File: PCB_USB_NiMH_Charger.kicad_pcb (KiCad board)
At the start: 2 copper layers, 94.9 x 72 mm, 45 parts, among them J1 USB_C_Receptacle_Simple, J2 Conn_02x01, J3 Conn_02x01, J4 Conn_02x01, Q1 2SA1015, Q2 2SC1815, Q3 2SB834, Q4 2SC1815, Q5 2SB834, U1 LM393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

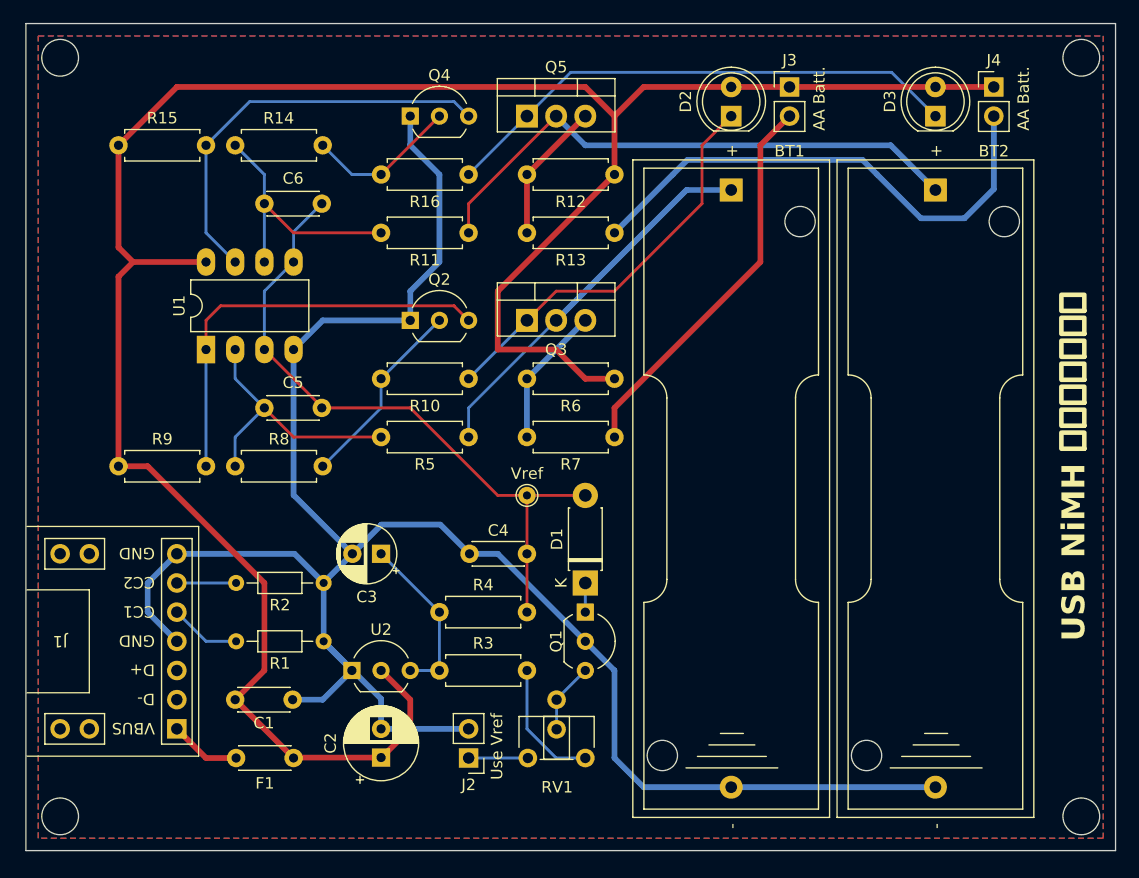
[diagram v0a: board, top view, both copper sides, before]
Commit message: WIP: Change 2-battery circuit to 4-battery circuit
Change LM393 to LM339.
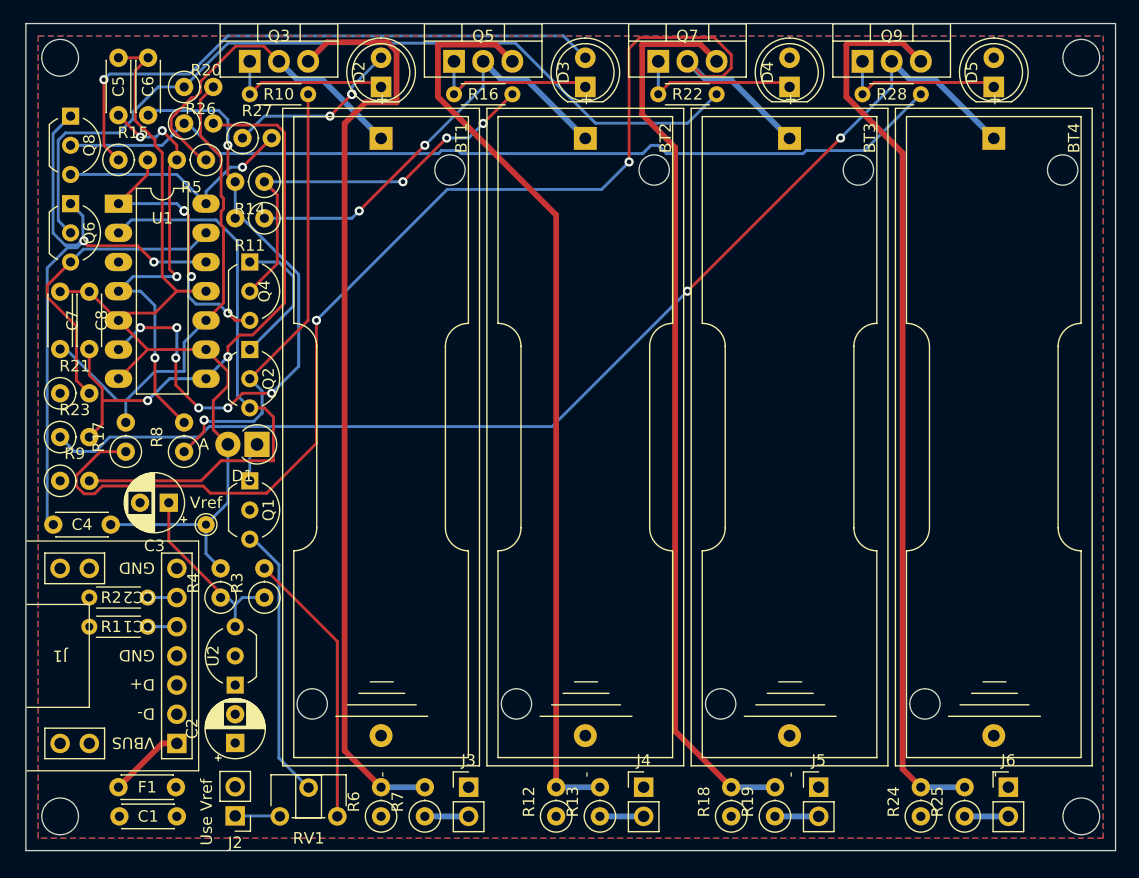
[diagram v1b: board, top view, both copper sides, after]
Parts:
- added BT3: Battery_Cell, Battery:BatteryHolder_Keystone_2460_1xAA, F.Cu at (91.4, 65.4)
- added BT4: Battery_Cell, Battery:BatteryHolder_Keystone_2460_1xAA, F.Cu at (109.2, 65.4)
- added C7: 0.1u, Capacitor_THT:C_Disc_D4.3mm_W1.9mm_P5.00mm, F.Cu at (27.9, 83.8)
- added C8: 0.1u, Capacitor_THT:C_Disc_D4.3mm_W1.9mm_P5.00mm, F.Cu at (30.5, 83.8)
- added D4: LED, LED_THT:LED_D5.0mm, F.Cu at (91.4, 61.0)
- added D5: LED, LED_THT:LED_D5.0mm, F.Cu at (109.2, 61.0)
- added J5: Conn_02x01, Connector_PinHeader_2.54mm:PinHeader_1x02_P2.54mm_Vertical, F.Cu at (94.0, 121.9)
- added J6: Conn_02x01, Connector_PinHeader_2.54mm:PinHeader_1x02_P2.54mm_Vertical, F.Cu at (110.5, 121.9)
- added Q6: 2SC1815, Package_TO_SOT_THT:TO-92_Inline_Wide, F.Cu at (28.9, 71.1)
- added Q7: 2SB834, Package_TO_SOT_THT:TO-220-3_Vertical, F.Cu at (80.0, 58.7)
- added Q8: 2SC1815, Package_TO_SOT_THT:TO-92_Inline_Wide, F.Cu at (28.9, 63.5)
- added Q9: 2SB834, Package_TO_SOT_THT:TO-220-3_Vertical, F.Cu at (97.8, 58.7)
- added R17: 10k, Resistor_THT:R_Axial_DIN0207_L6.3mm_D2.5mm_P2.54mm_Vertical, F.Cu at (33.7, 92.7)
- added R18: 15, Resistor_THT:R_Axial_DIN0207_L6.3mm_D2.5mm_P2.54mm_Vertical, F.Cu at (86.4, 124.5)
- added R19: 10, Resistor_THT:R_Axial_DIN0207_L6.3mm_D2.5mm_P2.54mm_Vertical, F.Cu at (90.2, 124.5)
- added R20: 1M, Resistor_THT:R_Axial_DIN0207_L6.3mm_D2.5mm_P2.54mm_Vertical, F.Cu at (38.7, 61.0)
- added R21: 10k, Resistor_THT:R_Axial_DIN0207_L6.3mm_D2.5mm_P2.54mm_Vertical, F.Cu at (27.9, 87.6)
- added R22: 680, Resistor_THT:R_Axial_DIN0204_L3.6mm_D1.6mm_P5.08mm_Horizontal, F.Cu at (80.0, 61.6)
- added R23: 10k, Resistor_THT:R_Axial_DIN0207_L6.3mm_D2.5mm_P2.54mm_Vertical, F.Cu at (27.9, 91.4)
- added R24: 15, Resistor_THT:R_Axial_DIN0207_L6.3mm_D2.5mm_P2.54mm_Vertical, F.Cu at (102.9, 124.5)
- added R25: 10, Resistor_THT:R_Axial_DIN0207_L6.3mm_D2.5mm_P2.54mm_Vertical, F.Cu at (106.7, 124.5)
- added R26: 1M, Resistor_THT:R_Axial_DIN0207_L6.3mm_D2.5mm_P2.54mm_Vertical, F.Cu at (38.7, 64.1)
- added R27: 10k, Resistor_THT:R_Axial_DIN0207_L6.3mm_D2.5mm_P2.54mm_Vertical, F.Cu at (43.8, 65.4)
- added R28: 680, Resistor_THT:R_Axial_DIN0204_L3.6mm_D1.6mm_P5.08mm_Horizontal, F.Cu at (97.8, 61.6)
- C2: footprint Capacitor_THT:CP_Radial_D6.3mm_P2.50mm -> Capacitor_THT:CP_Radial_D5.0mm_P2.50mm
- D1: footprint Diode_THT:D_DO-41_SOD81_P7.62mm_Horizontal -> Diode_THT:D_DO-41_SOD81_P2.54mm_Vertical_AnodeUp
- R1, R2: footprint Resistor_THT:R_Axial_DIN0204_L3.6mm_D1.6mm_P7.62mm_Horizontal -> Resistor_THT:R_Axial_DIN0204_L3.6mm_D1.6mm_P5.08mm_Horizontal
- R10, R16: footprint Resistor_THT:R_Axial_DIN0207_L6.3mm_D2.5mm_P7.62mm_Horizontal -> Resistor_THT:R_Axial_DIN0204_L3.6mm_D1.6mm_P5.08mm_Horizontal
- R11, R12, R13, R14, R15, R3, R4, R5, R6, R7, R8, R9: footprint Resistor_THT:R_Axial_DIN0207_L6.3mm_D2.5mm_P7.62mm_Horizontal -> Resistor_THT:R_Axial_DIN0207_L6.3mm_D2.5mm_P2.54mm_Vertical
- RV1: footprint mylib:Potentiometer_ACP_CA6-H2-3,5_Horizontal -> Potentiometer_THT:Potentiometer_ACP_CA6-H2,5_Horizontal
- U1: value LM393 -> LM339; footprint Package_DIP:DIP-8_W7.62mm_LongPads -> Package_DIP:DIP-14_W7.62mm_LongPads
- moved J4 68.2 mm to (78.7, 121.9)
- moved J3 67.1 mm to (63.5, 121.9)
- moved R12 56.1 mm to (71.1, 124.5), turned to 90 degrees
- moved R13 50.8 mm to (74.9, 124.5), turned to 90 degrees
- moved R6 43.2 mm to (55.9, 124.5), turned to 90 degrees
- moved R7 36.9 mm to (59.7, 124.5), turned to 90 degrees
- moved C4 36.3 mm to (32.3, 99.1)
- moved R5 33.2 mm to (40.6, 67.3)
- moved Q3 33.0 mm to (44.5, 58.7)
- moved Q1 31.4 mm to (44.5, 95.2)
- moved R10 31.2 mm to (44.5, 61.6), turned to 0 degrees
- moved D1 31.0 mm to (45.1, 92.1), turned to 180 degrees
- moved BT2 30.8 mm to (73.7, 65.4)
- moved BT1 30.8 mm to (55.9, 65.4)
- moved D3 30.6 mm to (73.7, 61.0)
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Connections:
- U1 pad 1: Net-(Q2-B) -> Net-(Q4-B)
- U1 pad 2: Net-(U1A--) -> Net-(Q2-B)
- U1 pad 3: Vref -> +5V
- U1 pad 4: GND -> Net-(U1A--)
- U1 pad 7: Net-(Q4-B) -> Vref
- U1 pad 8: +5V -> Net-(U1D--)
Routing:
- net +5V: track 204.1 -> 67.1 mm, vias 0 -> 4
- net Net-(BT3-+): track 0.00 -> 110.5 mm, vias 0 -> 2
- net GND: track 176.1 -> 68.2 mm, vias 0 -> 2
- net Net-(BT4-+): track 0.00 -> 100.0 mm, vias 0 -> 2
- net Net-(Q8-C): track 0.00 -> 78.9 mm
- net Net-(Q7-E): track 0.00 -> 78.8 mm
- net Net-(Q9-E): track 0.00 -> 78.3 mm
- net Net-(Q6-C): track 0.00 -> 73.6 mm
- net Net-(Q3-E): track 12.3 -> 81.4 mm
- net Net-(Q5-E): track 12.3 -> 79.8 mm
- net Net-(U1D--): track 0.00 -> 49.7 mm, vias 0 -> 2
- net Net-(U1C--): track 0.00 -> 43.3 mm
- net Net-(J4-Pin_2): track 45.2 -> 3.81 mm
- net Net-(U1B--): track 22.4 -> 55.8 mm, vias 0 -> 7
- net Net-(D3-K): track 45.9 -> 14.9 mm
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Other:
- board text removed: "AA Batt."
- board text removed: "USB NiMH ゆっくり充電器"

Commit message: 配線一旦削除
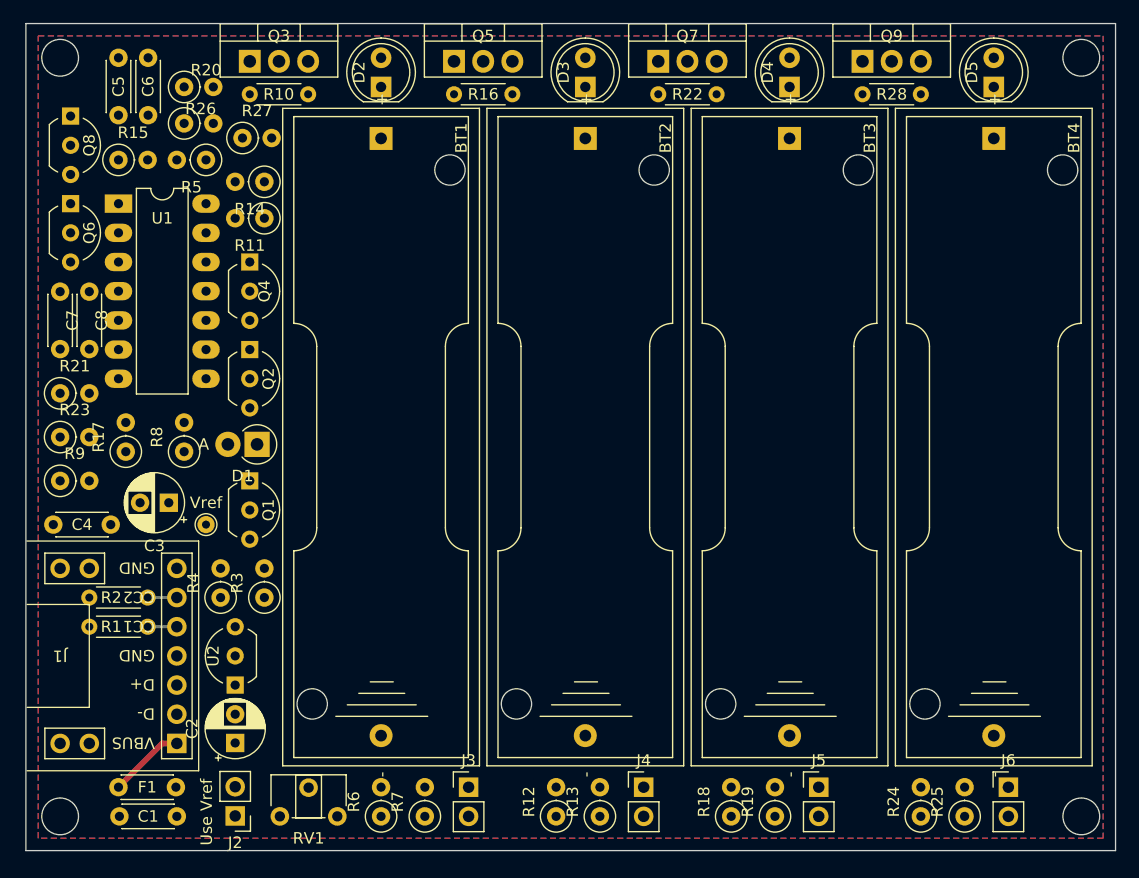
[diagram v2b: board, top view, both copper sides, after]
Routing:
- net Net-(BT3-+): track 110.5 -> 0.00 mm, vias 2 -> 0
- net Net-(BT4-+): track 100.0 -> 0.00 mm, vias 2 -> 0
- net Vref: track 82.4 -> 0.00 mm
- net Net-(Q3-E): track 81.4 -> 0.00 mm
- net Net-(Q5-E): track 79.8 -> 0.00 mm
- net Net-(Q8-C): track 78.9 -> 0.00 mm
- net Net-(Q7-E): track 78.8 -> 0.00 mm
- net Net-(Q9-E): track 78.3 -> 0.00 mm
- net Net-(Q6-C): track 73.6 -> 0.00 mm
- net GND: track 68.2 -> 0.00 mm, vias 2 -> 0
- net +5V: track 67.1 -> 0.00 mm, vias 4 -> 0
- net Net-(U1B--): track 55.8 -> 0.00 mm, vias 7 -> 0
- net Net-(U1D--): track 49.7 -> 0.00 mm, vias 2 -> 0
- net Net-(Q2-B): track 49.5 -> 0.00 mm
- net Net-(U1C--): track 43.3 -> 0.00 mm
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
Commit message: Change BT1 and BT2 to AAA from AA
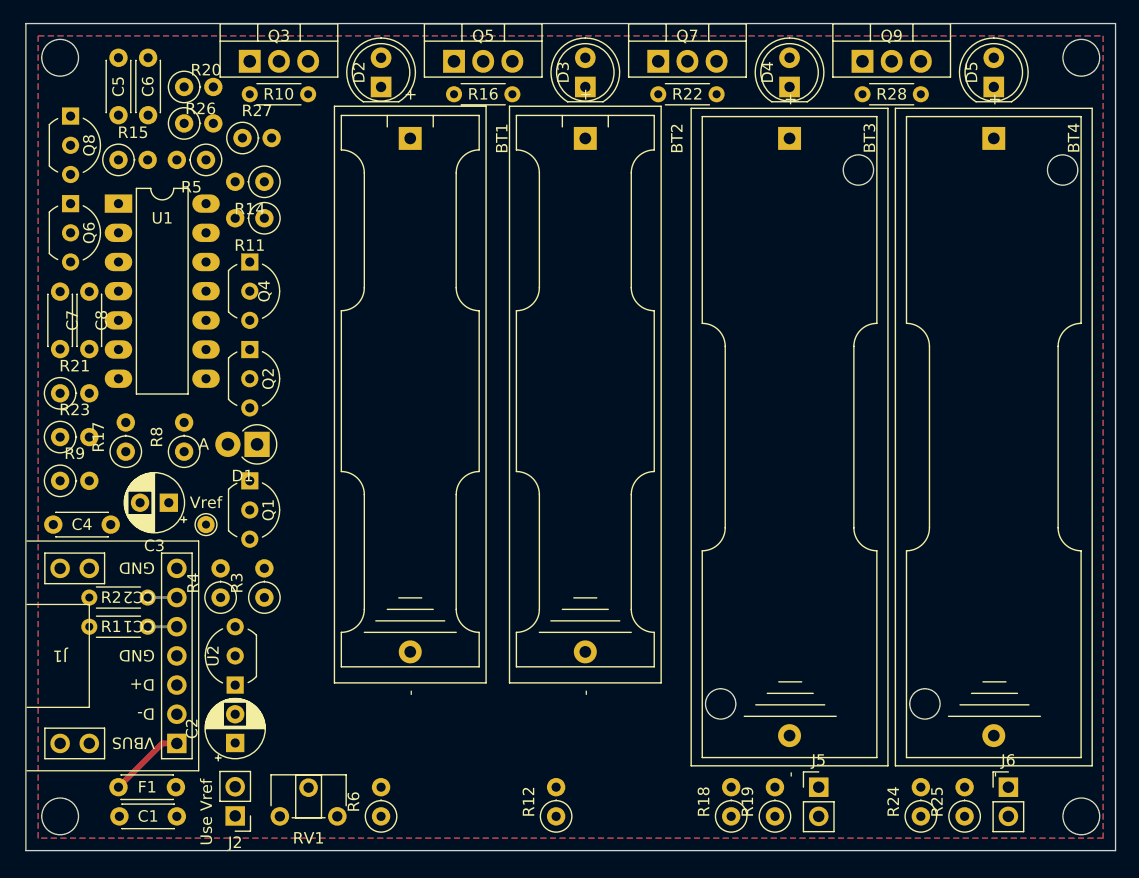
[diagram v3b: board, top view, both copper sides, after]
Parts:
- removed J3, J4: Conn_02x01, Connector_PinHeader_2.54mm:PinHeader_1x02_P2.54mm_Vertical
- removed R13, R7: 10, Resistor_THT:R_Axial_DIN0207_L6.3mm_D2.5mm_P2.54mm_Vertical
- BT1, BT2: footprint Battery:BatteryHolder_Keystone_2460_1xAA -> Battery:BatteryHolder_Keystone_2466_1xAAA
- moved BT1 2.54 mm to (58.4, 65.4)

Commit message: Update
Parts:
- removed J5, J6: Conn_02x01, Connector_PinHeader_2.54mm:PinHeader_1x02_P2.54mm_Vertical
- removed R18, R24: 15, Resistor_THT:R_Axial_DIN0207_L6.3mm_D2.5mm_P2.54mm_Vertical
- BT1, BT2: value Battery_Cell -> Battery_Cell (AAA)
- BT3, BT4: value Battery_Cell -> Battery_Cell (AA)
- C2, C3: footprint Capacitor_THT:CP_Radial_D5.0mm_P2.50mm -> Capacitor_THT:CP_Radial_D5.0mm_P2.00mm
- J1: footprint mylib:Connector_USB_C_simple -> mylib:USB_C_Receptacle_CUI_Devices_UJC-HP-3-SMT-TR
- Q2, Q4, Q6, Q8: value 2SC1815 -> 2SC2458; footprint Package_TO_SOT_THT:TO-92_Inline_Wide -> Package_TO_SOT_THT:TO-92S_Wide
- R1, R2: footprint Resistor_THT:R_Axial_DIN0204_L3.6mm_D1.6mm_P5.08mm_Horizontal -> Resistor_THT:R_Axial_DIN0204_L3.6mm_D1.6mm_P2.54mm_Vertical
- moved R2 13.7 mm to (38.1, 116.8), turned to 180 degrees
- moved R1 9.92 mm to (38.1, 114.3), turned to 180 degrees
- moved J1 9.28 mm to (29.3, 115.1), turned to -90 degrees
- moved BT1 6.24 mm to (58.4, 71.7)
- moved BT2 6.24 mm to (73.7, 71.7)
- moved C3 5.76 mm to (38.1, 102.9)
- moved C1 0.08 mm to (33.0, 124.5)
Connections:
- C7 pad 2: Vref -> Net-(U1C-+)
- F1 pad 2: Net-(F1-Pad2) -> /VBUS
- R19 pad 1: Net-(J5-Pin_2) -> +5V
- R25 pad 1: Net-(J6-Pin_2) -> +5V
- U1 pad 11: Vref -> Net-(U1C-+)
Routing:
- net /VBUS: track 0.00 -> 12.1 mm
- net GND: track 0.00 -> 8.86 mm, vias 0 -> 2
- net Net-(F1-Pad2): track 6.66 -> 0.00 mm
- net Net-(J1-CC2): track 2.54 -> 4.66 mm
- net Net-(J1-CC1): track 2.54 -> 4.24 mm
